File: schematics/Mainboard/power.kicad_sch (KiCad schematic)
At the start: 21 parts, among them J7 Battery

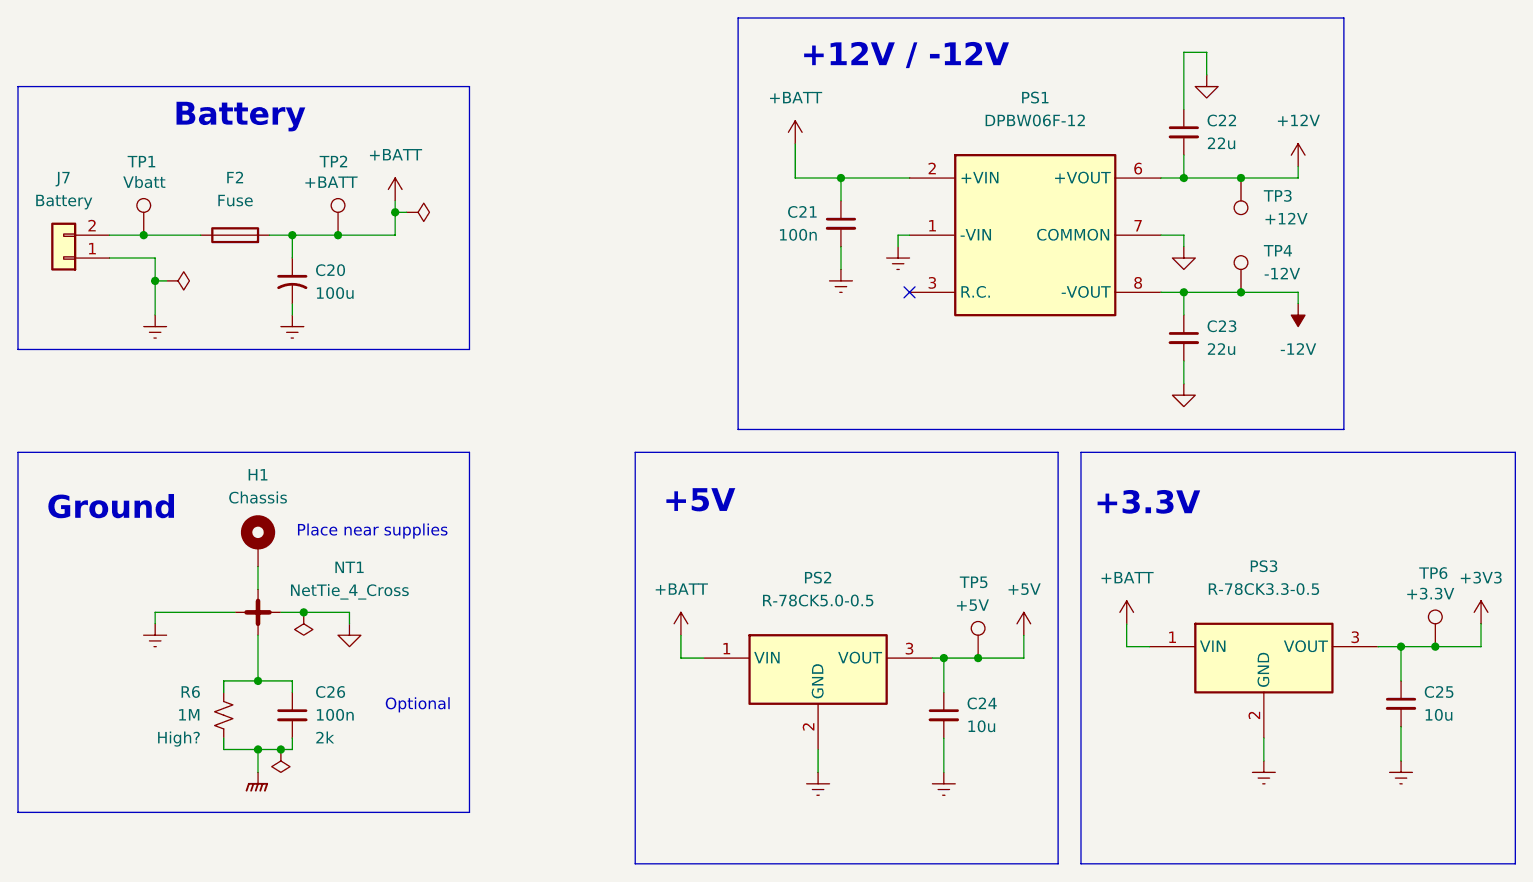
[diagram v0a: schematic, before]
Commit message: feat(mainboard): Finished mainboard part selection
Signed-off-by: Andrew Balmos <abalmos@purdue.edu>
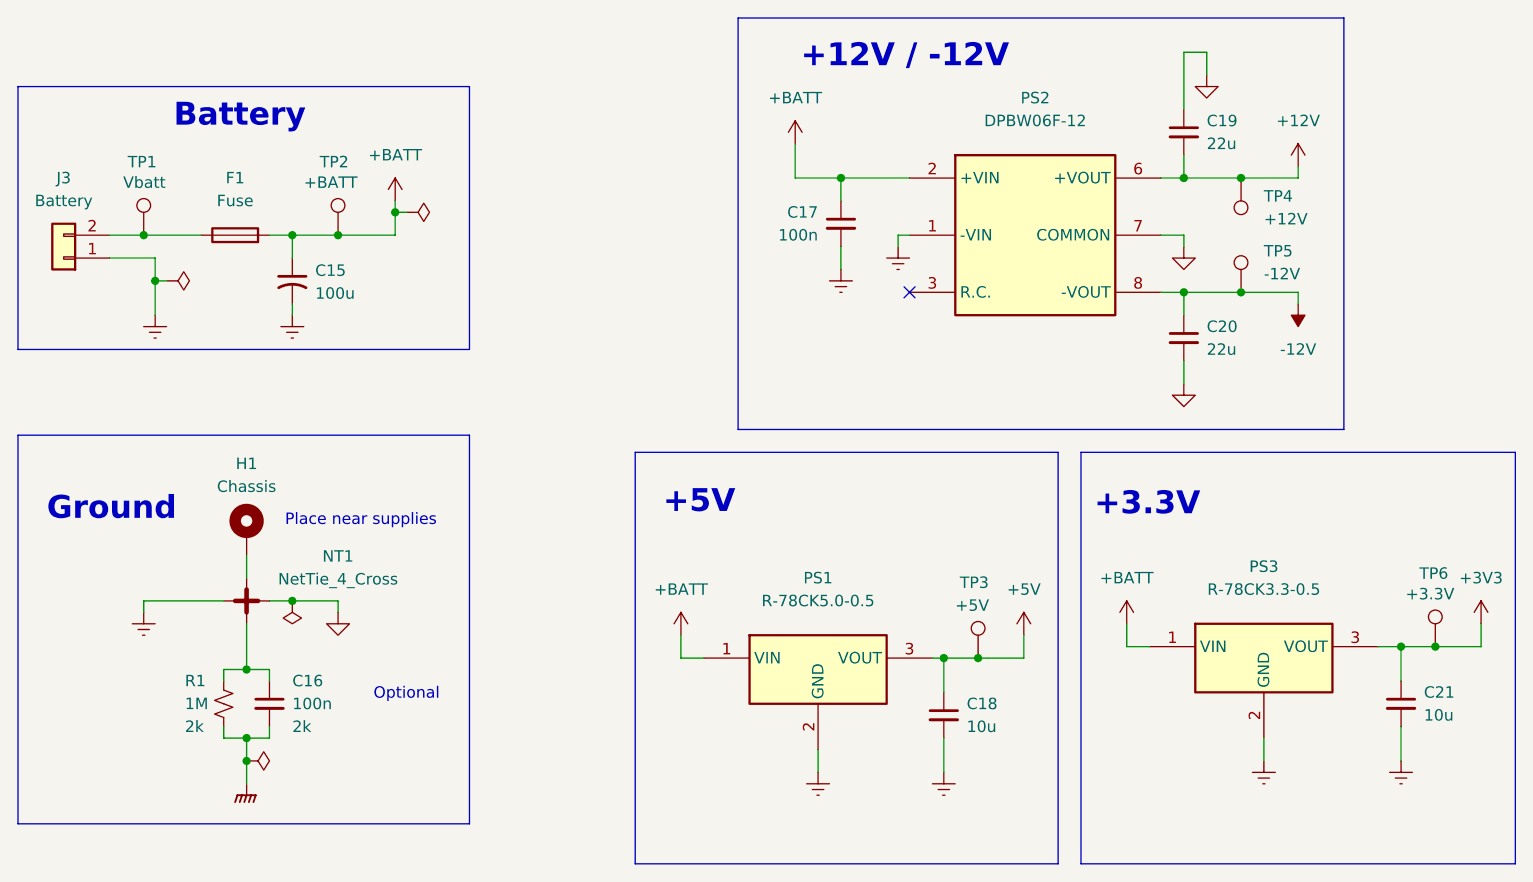
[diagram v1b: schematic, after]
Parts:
- C15: renamed from C20; footprint (none) -> Capacitor_SMD:C_Elec_6.3x7.7; LCSC (none) -> C72478; MPN (none) -> RVT1V101M0607
- C16: renamed from C26; footprint (none) -> Capacitor_SMD:C_2220_5750Metric; LCSC (none) -> C5290327; MPN (none) -> FV55X104K202EGG
- C17: renamed from C21; footprint (none) -> Capacitor_SMD:C_0603_1608Metric; LCSC (none) -> C6119867; MPN (none) -> CGA0603X7R104K500JT
- C18: renamed from C24; footprint (none) -> Capacitor_SMD:C_0805_2012Metric; LCSC (none) -> C32635; MPN (none) -> CL21B106KPQNNNE
- C19: renamed from C22; footprint (none) -> Capacitor_SMD:C_2220_5750Metric; LCSC (none) -> C784103; MPN (none) -> FS55X226K500EHG
- C20: renamed from C23; footprint (none) -> Capacitor_SMD:C_2220_5750Metric; LCSC (none) -> C784103; MPN (none) -> FS55X226K500EHG
- C21: renamed from C25; footprint (none) -> Capacitor_SMD:C_0805_2012Metric; LCSC (none) -> C32635; MPN (none) -> CL21B106KPQNNNE
- F1: renamed from F2; LCSC (none) -> C206910; MPN (none) -> 0154002.DR
- J3: renamed from J7; footprint (none) -> Link_Footprints:TE_3-641215-2; DigiKey (none) -> A30786-ND; LCSC (none) -> C5168872; MPN (none) -> 3-641215-2
- NT1: footprint (none) -> NetTie:NetTie-4_SMD_Pad2.0mm
- R1: renamed from R6; footprint (none) -> Resistor_SMD:R_2010_5025Metric; LCSC (none) -> C1513439; MPN (none) -> RCV20101M00FKEFAT; Volt High? -> 2k
- TP1, TP2, TP6: footprint (none) -> TestPoint:TestPoint_Pad_D2.0mm
- TP3: renamed from TP5; footprint (none) -> TestPoint:TestPoint_Pad_D2.0mm
- TP4: renamed from TP3; footprint (none) -> TestPoint:TestPoint_Pad_D2.0mm
- TP5: renamed from TP4; footprint (none) -> TestPoint:TestPoint_Pad_D2.0mm
- renumbered PS2 to PS1, PS1 to PS2
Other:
- moved on the sheet: C16, H1, NT1, R1

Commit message: release(mainboard): v1.0. Ordered.
Signed-off-by: Andrew Balmos <abalmos@purdue.edu>
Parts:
- removed NT1: NetTie_4_Cross, NetTie:NetTie-4_SMD_Pad2.0mm, symbol Device:NetTie_4_Cross
- added NT1: NetTie_3_Tee, NetTie:NetTie-3_SMD_Pad2.0mm, symbol Device:NetTie_3_Tee
- added TP7: GND, Link_Footprints:TestPoint_Pad_D1.5mm, symbol Connector:TestPoint
- C15: footprint Capacitor_SMD:C_Elec_6.3x7.7 -> Capacitor_SMD:CP_Elec_6.3x5.4; FT Rotation Offset (none) -> 180; LCSC C72478 -> C4747964; MPN RVT1V101M0607 -> RST100UF25V004
- H1: footprint (none) -> MountingHole:MountingHole_4.3mm_M4_Pad_TopOnly
- PS1, PS2, PS3: now not fitted
- TP1, TP2, TP3, TP4, TP5, TP6: footprint TestPoint:TestPoint_Pad_D2.0mm -> Link_Footprints:TestPoint_Pad_D1.5mm; now left out of the parts list
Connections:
- net GND: now also NT1.2, TP7.1
- net GNDBATT: now also NT1.1
- net GNDPWR: now also H1.1
- net at C16.1, R1.1: now also NT1.3
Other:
- note removed: "Optional"
- moved on the sheet: C16, H1, R1
